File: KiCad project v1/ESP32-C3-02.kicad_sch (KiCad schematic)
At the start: 0 parts

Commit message: Starting integration of the ESP32.
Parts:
- added U3: ESP32-C3-WROOM-02-H4, ESP32-C3-WROOM-02-H4:MODULE_ESP32-C3-WROOM-02-H4, symbol ESP32-C3-WROOM-02-H4:ESP32-C3-WROOM-02-H4
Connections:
- new net: U3.19 (GND), U3.20 (GND), U3.21 (GND), U3.22 (GND), U3.23 (GND), U3.24 (GND), U3.25 (GND), U3.26 (GND), U3.27 (GND), U3.28 (GND), U3.29 (GND), U3.30 (GND), U3.31 (GND), U3.32 (GND), U3.33 (GND), U3.34 (GND), U3.35 (GND), U3.36 (GND), U3.37 (GND), U3.38 (GND), U3.39 (GND), U3.9 (GND)
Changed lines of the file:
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@@
 	(generator_version "8.0")
 	(paper "A4")
+	(symbol
+		(lib_id "ESP32-C3-WROOM-02-H4:ESP32-C3-WROOM-02-H4")
+		(at 137.16 96.52 0)
+		(unit 1)
+		(exclude_from_sim no)
+		(in_bom yes)
+		(on_board yes)
+		(dnp no)
+		(fields_autoplaced yes)
+		(property "Reference" "U3"
+			(at 137.16 71.12 0)
+			(effects
+				(font
+					(size 1.27 1.27)
+				)
+			)
+		)
+		(property "Value" "ESP32-C3-WROOM-02-H4"
+			(at 137.16 73.66 0)
+			(effects
+				(font
+					(size 1.27 1.27)
+				)
+			)
+		)
+		(property "Footprint" "ESP32-C3-WROOM-02-H4:MODULE_ESP32-C3-WROOM-02-H4"
+			(at 137.16 96.52 0)
+			(effects
+				(font
+					(size 1.27 1.27)
+				)
+				(justify bottom)
+				(hide yes)
+			)
+		)
+		(property "Datasheet" ""
+			(at 137.16 96.52 0)
+			(effects
+				(font
+					(size 1.27 1.27)
+				)
+				(hide yes)
+			)
+		)
+		(property "Description" ""
+			(at 137.16 96.52 0)
+			(effects
+				(font
+					(size 1.27 1.27)
+				)
+				(hide yes)
+			)
+		)
+		(property "MF" "Espressif Systems"
+			(at 137.16 96.52 0)
+			(effects
+				(font
+					(size 1.27 1.27)
+				)
+				(justify bottom)
+				(hide yes)
+			)
+		)
+		(property "Description_1" "\n                        \n                            WiFi Modules (802.11) (Engineering Samples) SMD module, ESP32-C3, 4MB SPI flash, PCB antenna, -40 C +105 C\n                        \n"
+			(at 137.16 96.52 0)
+			(effects
+				(font
+					(size 1.27 1.27)
+				)
+				(justify bottom)
+				(hide yes)
+			)
+		)
+		(property "Package" "Package"
+			(at 137.16 96.52 0)
+			(effects
+				(font
+					(size 1.27 1.27)
+				)
+				(justify bottom)
+				(hide yes)
+			)
+		)
+		(property "Price" "None"
+			(at 137.16 96.52 0)
+			(effects
+				(font
+					(size 1.27 1.27)
+				)
+				(justify bottom)
+				(hide yes)
+			)
+		)
+		(property "Check_prices" "https://www.snapeda.com/parts/ESP32-C3-WROOM-02-H4/Espressif+Systems/view-part/?ref=eda"
+			(at 137.16 96.52 0)
+			(effects
+				(font
+					(size 1.27 1.27)
+				)
+				(justify bottom)
+				(hide yes)
+			)
+		)
+		(property "SnapEDA_Link" "https://www.snapeda.com/parts/ESP32-C3-WROOM-02-H4/Espressif+Systems/view-part/?ref=snap"
+			(at 137.16 96.52 0)
+			(effects
+				(font
+					(size 1.27 1.27)
+				)
+				(justify bottom)
+				(hide yes)
+			)
+		)
+		(property "MP" "ESP32-C3-WROOM-02-H4"
+			(at 137.16 96.52 0)
+			(effects
+				(font
+					(size 1.27 1.27)
+				)
+				(justify bottom)
+				(hide yes)
+			)
+		)
+		(property "Availability" "In Stock"
+			(at 137.16 96.52 0)
+			(effects
+				(font
+					(size 1.27 1.27)
+				)
+				(justify bottom)
+				(hide yes)
+			)
+		)
+		(property "Purchase-URL" "https://pricing.snapeda.com/search/part/ESP32-C3-WROOM-02-H4/?ref=eda"
+			(at 137.16 96.52 0)
+			(effects
+				(font
+					(size 1.27 1.27)
+				)
+				(justify bottom)
+				(hide yes)
+			)
+		)
+		(pin "30"
+		)
+		(pin "5"
+		)
+		(pin "7"
+		)
+		(pin "25"
+		)
+		(pin "24"
+		)
+		(pin "8"
+		)
+		(pin "9"
+		)
+		(pin "14"
+		)
+		(pin "26"
+		)
+		(pin "22"
+		)
+		(pin "23"
+		)
+		(pin "21"
+		)
+		(pin "13"
+		)
+		(pin "17"
+		)
+		(pin "34"
+		)
+		(pin "4"
+		)
+		(pin "11"
+		)
+		(pin "36"
+		)
+		(pin "6"
+		)
+		(pin "12"
+		)
+		(pin "10"
+		)
+		(pin "35"
+		)
+		(pin "27"
+		)
+		(pin "28"
+		)
+		(pin "31"
+		)
+		(pin "3"
+		)
+		(pin "37"
+		)
+		(pin "29"
+		)
+		(pin "1"
+		)
+		(pin "19"
+		)
+		(pin "32"
+		)
+		(pin "20"
+		)
+		(pin "2"
+		)
+		(pin "16"
+		)
+		(pin "38"
+		)
+		(pin "39"
+		)
+		(pin "18"
+		)
+		(pin "15"
+		)
+		(pin "33"
+		)
+		(instances
+			(project ""
+				(path "/16c571a0-8550-4f05-972c-22b0701cbf02/09ec4a32-ddff-43cd-8e21-9ef822101853"
+					(reference "U3")
+					(unit 1)
+				)
+			)
+		)
+	)
 )

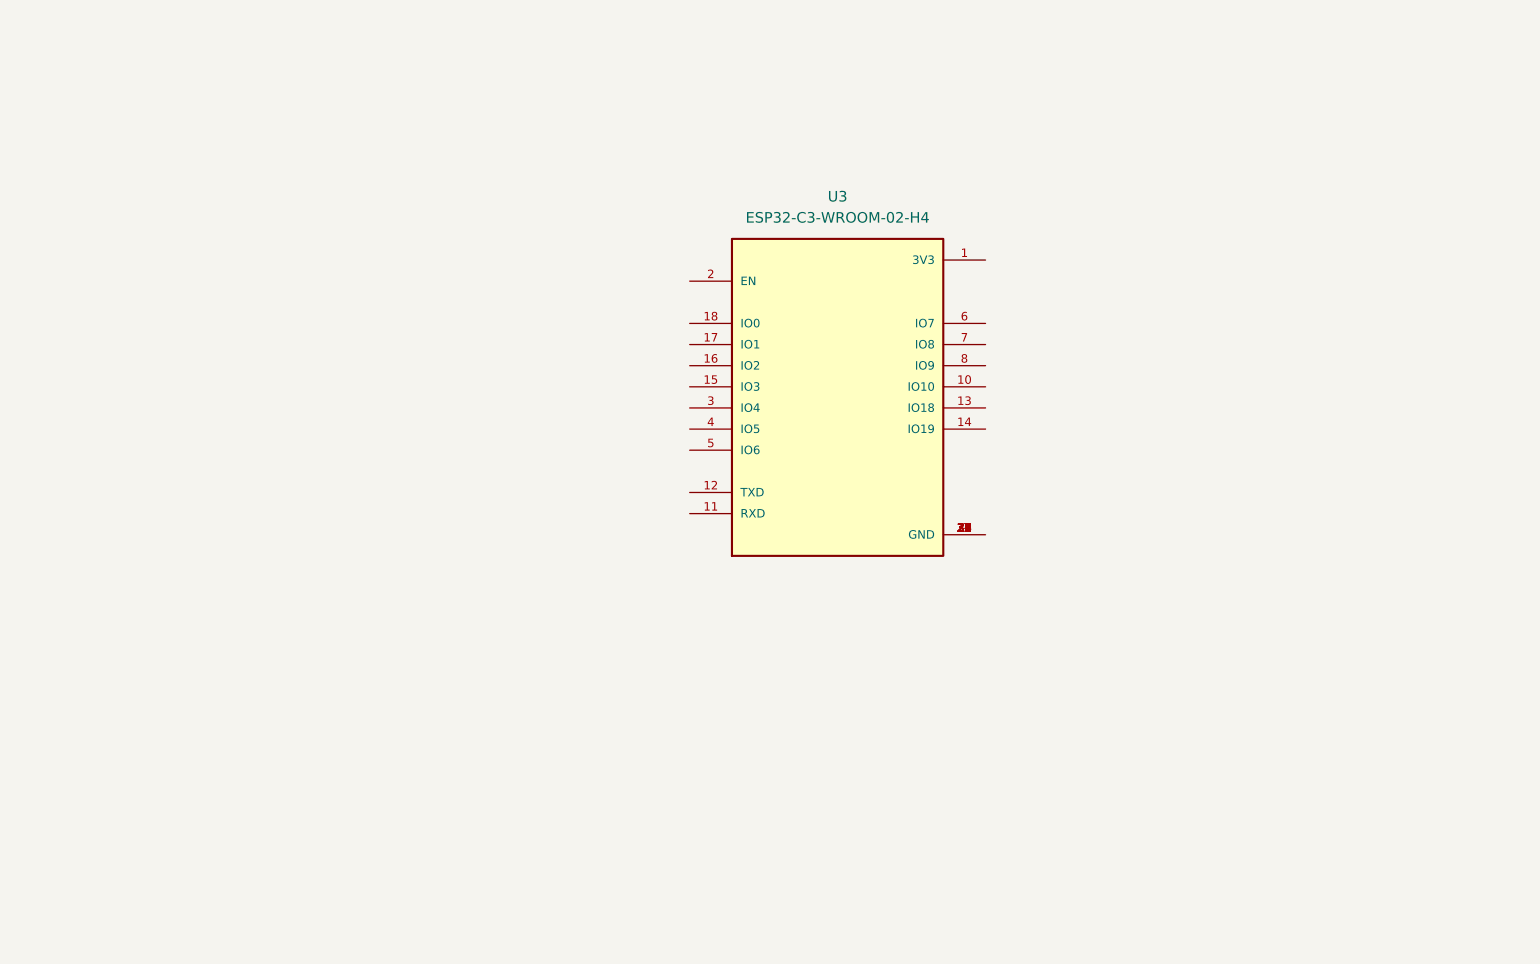
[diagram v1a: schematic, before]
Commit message: Completed first revision of the ESP32 and CP2102 integration.
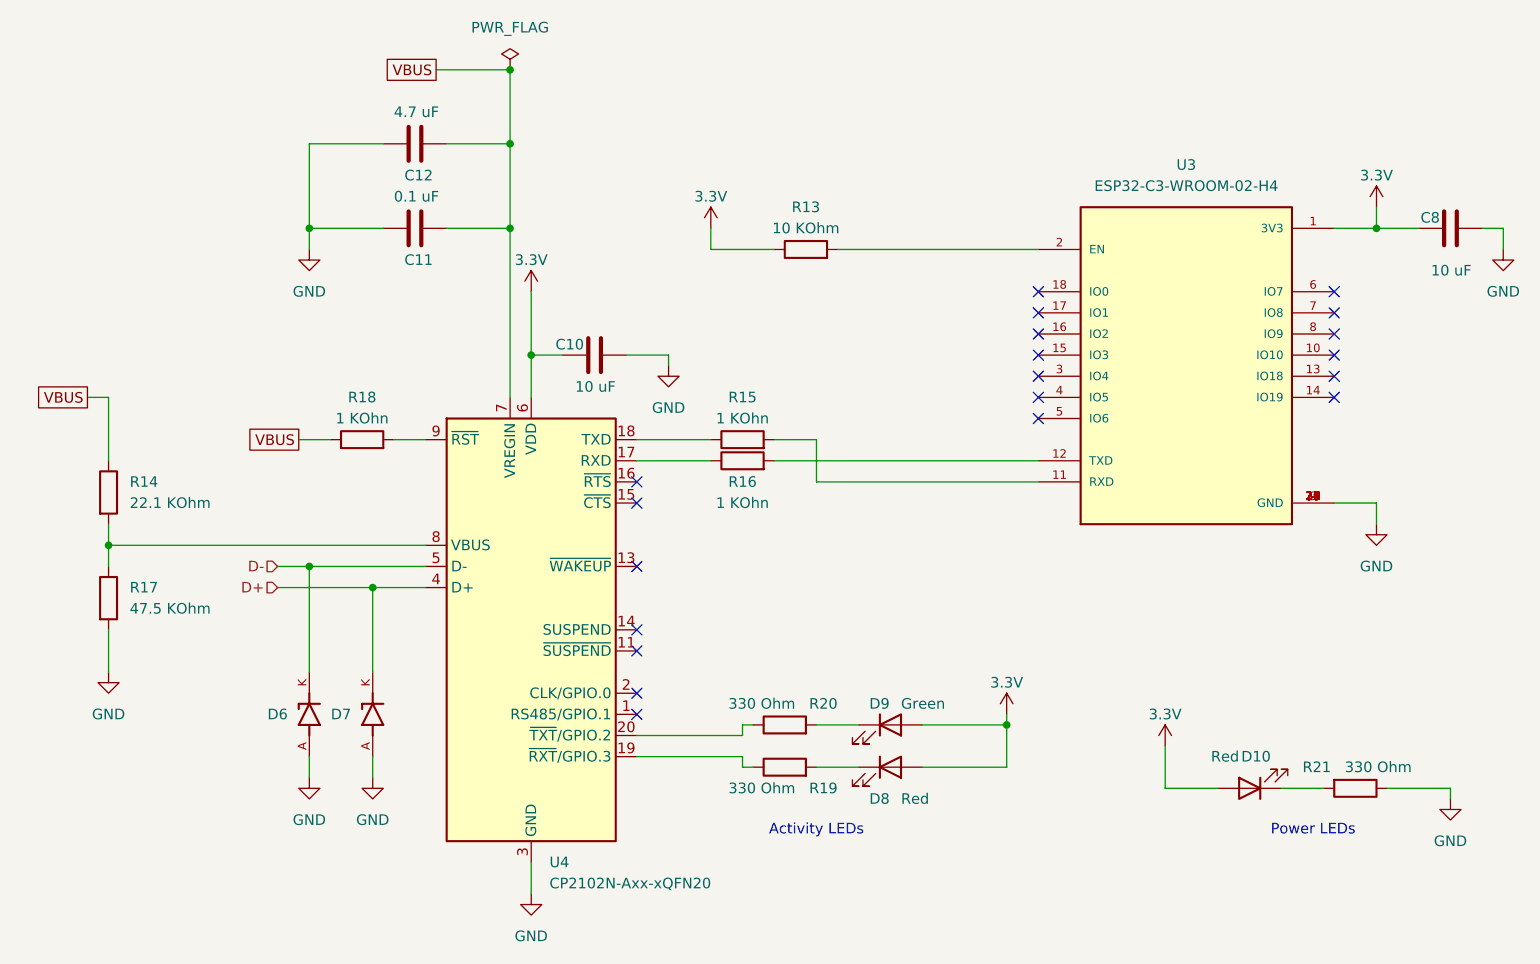
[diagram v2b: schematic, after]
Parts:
- added C10, C8: 10 uF, Capacitor_SMD:C_0805_2012Metric, symbol SparkFun-Capacitor:C
- added C11: 0.1 uF, Capacitor_SMD:C_0805_2012Metric, symbol SparkFun-Capacitor:C
- added C12: 4.7 uF, Capacitor_SMD:C_0805_2012Metric, symbol SparkFun-Capacitor:C
- added D10, D8: Red, SparkFun-LED:LED_0603_1608Metric, symbol SparkFun-LED:LED_Red_0603
- added D6, D7: PESD5V0S1UL_315, PESD5V0S1UL_315:DIO_PESD5V0S1UL_315, symbol PESD5V0S1UL_315:PESD5V0S1UL_315
- added D9: Green, SparkFun-LED:LED_0603_1608Metric, symbol SparkFun-LED:LED_Green_0603
- added R13: 10 KOhm, symbol Device:R
- added R14: 22.1 KOhm, symbol Device:R
- added R15, R16, R18: 1 KOhn, symbol Device:R
- added R17: 47.5 KOhm, symbol Device:R
- added R19, R20, R21: 330 Ohm, symbol Device:R
- added U4: CP2102N-Axx-xQFN20, Package_DFN_QFN:SiliconLabs_QFN-20-1EP_3x3mm_P0.5mm, symbol Interface_USB:CP2102N-Axx-xQFN20
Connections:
- net 3.3V: now reaches U3.1 (3V3)
- net 3.3V: now also C10.1, C8.1, D10.2 (A), D8.2 (A), D9.2 (A), R13.1, U4.6 (VDD)
- net at U3.11 (RXD): now also R15.2
- net at U3.12 (TXD): now also R16.2
- net GND: now reaches U3.19 (GND), U3.20 (GND), U3.21 (GND), U3.22 (GND), U3.23 (GND), U3.24 (GND), U3.25 (GND), U3.26 (GND), U3.27 (GND), U3.28 (GND), U3.29 (GND), U3.30 (GND), U3.31 (GND), U3.32 (GND), U3.33 (GND), U3.34 (GND), U3.35 (GND), U3.36 (GND), U3.37 (GND), U3.38 (GND), U3.39 (GND), U3.9 (GND)
- net GND: now also C10.2, C11.2, C12.2, C8.2, D6.A, D7.A, R17.2, R21.1, U4.12 (GND), U4.21 (GND), U4.3 (GND)
- net at U3.2 (EN): now also R13.2
- new net: D8.1 (K), R19.2
- new net: R14.2, R17.1, U4.8 (VBUS)
- new net: D10.1 (K), R21.2
- new net: R15.1, U4.18 (TXD)
- new net: R16.1, U4.17 (RXD)
- new net: R20.1, U4.20 (~{TXT}/GPIO.2)
- new net: D9.1 (K), R20.2
- new net: R19.1, U4.19 (~{RXT}/GPIO.3)
- new net: R18.2, U4.9 (~{RST})
- new net D+: D7.K, U4.4 (D+)
- new net D-: D6.K, U4.5 (D-)
- new net VBUS: C11.1, C12.1, R14.1, R18.1, U4.7 (VREGIN)
- no-connect marks 0 -> 20
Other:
- note added: "Activity LEDs"
- note added: "Power LEDs"
- company: (none) -> Tech Explorations
- title: (none) -> ESP32 C3 02 and USB to UART converter
- moved on the sheet: U3

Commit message: Created the draft layout, and inserted available footprints.
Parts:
- D6, D7: footprint PESD5V0S1UL_315:DIO_PESD5V0S1UL_315 -> Footprints:DIO_PESD5V0S1UL_315
- R13, R14, R15, R16, R17, R18, R19, R20, R21: footprint (none) -> Resistor_SMD:R_0805_2012Metric
- U3: footprint ESP32-C3-WROOM-02-H4:MODULE_ESP32-C3-WROOM-02-H4 -> Footprints:MODULE_ESP32-C3-WROOM-02-H4
- U4: footprint Package_DFN_QFN:SiliconLabs_QFN-20-1EP_3x3mm_P0.5mm -> Package_DFN_QFN:SiliconLabs_QFN-20-1EP_3x3mm_P0.5mm_EP1.8x1.8mm
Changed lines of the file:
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@@
 			)
 		)
-		(property "Footprint" "PESD5V0S1UL_315:DIO_PESD5V0S1UL_315"
+		(property "Footprint" "Footprints:DIO_PESD5V0S1UL_315"
 			(at 73.66 133.35 0)
 			(effects
@@
 			)
 		)
-		(property "Footprint" ""
+		(property "Footprint" "Resistor_SMD:R_0805_2012Metric"
 			(at 133.35 79.248 90)
 			(effects
@@
 			)
 		)
-		(property "Footprint" ""
+		(property "Footprint" "Resistor_SMD:R_0805_2012Metric"
 			(at 47.752 106.68 90)
 			(effects
@@
 			)
 		)
-		(property "Footprint" ""
+		(property "Footprint" "Resistor_SMD:R_0805_2012Metric"
 			(at 199.39 140.462 90)
 			(effects
@@
 			)
 		)
-		(property "Footprint" ""
+		(property "Footprint" "Resistor_SMD:R_0805_2012Metric"
 			(at 125.73 102.108 90)
 			(effects
@@
 			)
 		)
-		(property "Footprint" ""
+		(property "Footprint" "Resistor_SMD:R_0805_2012Metric"
 			(at 125.73 104.648 90)
 			(effects
@@
 			)
 		)
-		(property "Footprint" ""
+		(property "Footprint" "Resistor_SMD:R_0805_2012Metric"
 			(at 47.752 119.38 90)
 			(effects
@@
 			)
 		)
-		(property "Footprint" ""
+		(property "Footprint" "Resistor_SMD:R_0805_2012Metric"
 			(at 130.81 136.398 90)
 			(effects
@@
 			)
 		)
-		(property "Footprint" ""
+		(property "Footprint" "Resistor_SMD:R_0805_2012Metric"
 			(at 130.81 141.478 90)
 			(effects
@@
 			)
 		)
-		(property "Footprint" "Package_DFN_QFN:SiliconLabs_QFN-20-1EP_3x3mm_P0.5mm"
+		(property "Footprint" "Package_DFN_QFN:SiliconLabs_QFN-20-1EP_3x3mm_P0.5mm_EP1.8x1.8mm"
 			(at 132.08 149.86 0)
 			(effects
@@
 			)
 		)
-		(property "Footprint" "ESP32-C3-WROOM-02-H4:MODULE_ESP32-C3-WROOM-02-H4"
+		(property "Footprint" "Footprints:MODULE_ESP32-C3-WROOM-02-H4"
 			(at 179.07 92.71 0)
 			(effects
@@
 			)
 		)
-		(property "Footprint" ""
+		(property "Footprint" "Resistor_SMD:R_0805_2012Metric"
 			(at 80.01 102.108 90)
 			(effects
@@
 			)
 		)
-		(property "Footprint" "PESD5V0S1UL_315:DIO_PESD5V0S1UL_315"
+		(property "Footprint" "Footprints:DIO_PESD5V0S1UL_315"
 			(at 81.28 133.35 0)
 			(effects
